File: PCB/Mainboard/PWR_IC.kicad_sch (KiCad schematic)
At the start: 24 parts, among them U6 TPS62933, U7 TPS62933

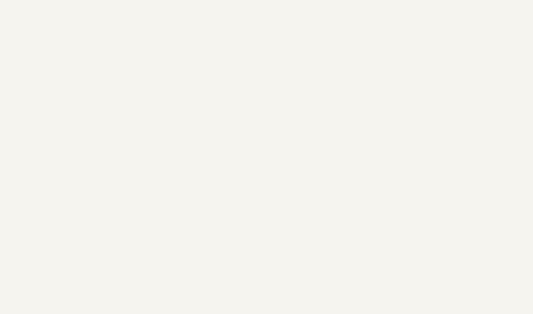
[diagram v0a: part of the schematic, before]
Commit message: Added setup, read and get Command
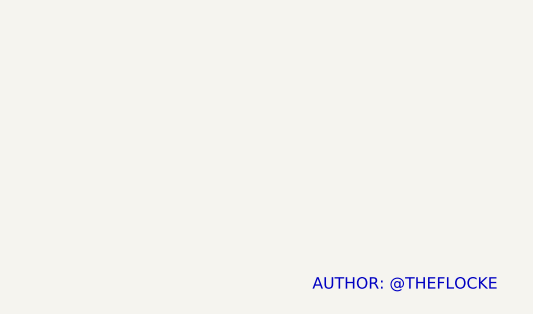
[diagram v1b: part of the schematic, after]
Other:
- note added: "AUTHOR: @THEFLOCKE"
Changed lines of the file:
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@@
+		)
+	)
+	(text "AUTHOR: @THEFLOCKE"
+		(exclude_from_sim no)
+		(at 249.936 196.596 0)
+		(effects
+			(font
+				(face "KiCad Font")
+				(size 1.27 1.27)
+				(color 194 0 194 1)
+			)
 		)
 	)
